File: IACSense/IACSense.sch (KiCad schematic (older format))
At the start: 61 parts, among them P1 IN, P2 OUT, P3 zcd, P4 event, P5 Prog, P6 nRF24L01+, P7 I2C, U1 MCP39F521, U2 MCP970x, U3 MCP1754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

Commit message: Update IACSense
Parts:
- added C21: 10u, Yame_library:SM0805-MR, symbol C
- added FB5: BLM18AG102SN1D, Yame_library:SM0603-MR, symbol FILTER
- R2: footprint Yame_library:SM0603-MR -> Yame_library:SM1206-MR
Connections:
- wire segments 180 -> 186
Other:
- moved on the sheet: C16, C19, C20, R18

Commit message: Update IACSense
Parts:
- removed P7: I2C, Yame_library:HE10_14-3C-2.54-MR, symbol CONN_01X03
- added P7: I2C, Yame_library:HE10_14-4C-2.54-MR, symbol CONN_01X04
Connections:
- wire segments 186 -> 189
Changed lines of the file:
@@
 $EndComp
 $Comp
-L CONN_01X03 P7
-U 1 1 5676C8C1
-P 10650 950
-F 0 "P7" H 10650 1150 50  0000 C CNN
-F 1 "I2C" V 10750 950 50  0000 C CNN
-F 2 "Yame_library:HE10_14-3C-2.54-MR" H 10650 950 50  0001 C CNN
-F 3 "" H 10650 950 50  0000 C CNN
-	1    10650 950
-	1    0    0    -1
-$EndComp
-$Comp
 L CONN_01X05 P5
 U 1 1 5676C91A
@@
 	2750 2400 3150 2400
 $Comp
-L GND #PWR1
+L GND #PWR01
 U 1 1 56D34A90
 P 2700 1900
-F 0 "#PWR1" H 2700 1650 50  0001 C CNN
+F 0 "#PWR01" H 2700 1650 50  0001 C CNN
 F 1 "GND" H 2700 1750 50  0000 C CNN
 F 2 "" H 2700 1900 60  0000 C CNN
@@
 Connection ~ 4000 2450
 $Comp
-L GND #PWR3
+L GND #PWR02
 U 1 1 56D35186
 P 3750 2900
-F 0 "#PWR3" H 3750 2650 50  0001 C CNN
+F 0 "#PWR02" H 3750 2650 50  0001 C CNN
 F 1 "GND" H 3750 2750 50  0000 C CNN
 F 2 "" H 3750 2900 60  0000 C CNN
@@
 Connection ~ 3350 3250
 $Comp
-L GND #PWR2
+L GND #PWR03
 U 1 1 56D35ED8
 P 3350 3850
-F 0 "#PWR2" H 3350 3600 50  0001 C CNN
+F 0 "#PWR03" H 3350 3600 50  0001 C CNN
 F 1 "GND" H 3350 3700 50  0000 C CNN
 F 2 "" H 3350 3850 60  0000 C CNN
@@
 $EndComp
 $Comp
-L GND #PWR4
+L GND #PWR04
 U 1 1 56D366F0
 P 3950 4700
-F 0 "#PWR4" H 3950 4450 50  0001 C CNN
+F 0 "#PWR04" H 3950 4450 50  0001 C CNN
 F 1 "GND" H 3950 4550 50  0000 C CNN
 F 2 "" H 3950 4700 60  0000 C CNN
@@
 $EndComp
 $Comp
-L GND #PWR7
+L GND #PWR05
 U 1 1 56D36767
 P 4250 4700
-F 0 "#PWR7" H 4250 4450 50  0001 C CNN
+F 0 "#PWR05" H 4250 4450 50  0001 C CNN
 F 1 "GND" H 4250 4550 50  0000 C CNN
 F 2 "" H 4250 4700 60  0000 C CNN
@@
 $EndComp
 $Comp
-L GND #PWR12
+L GND #PWR06
 U 1 1 56D37BE1
 P 6000 2700
-F 0 "#PWR12" H 6000 2450 50  0001 C CNN
+F 0 "#PWR06" H 6000 2450 50  0001 C CNN
 F 1 "GND" H 6000 2550 50  0000 C CNN
 F 2 "" H 6000 2700 60  0000 C CNN
@@
 Connection ~ 5850 3550
 $Comp
-L GND #PWR8
+L GND #PWR07
 U 1 1 56D38721
 P 4900 4250
-F 0 "#PWR8" H 4900 4000 50  0001 C CNN
+F 0 "#PWR07" H 4900 4000 50  0001 C CNN
 F 1 "GND" H 4900 4100 50  0000 C CNN
 F 2 "" H 4900 4250 60  0000 C CNN
@@
 $EndComp
 $Comp
-L GND #PWR9
+L GND #PWR08
 U 1 1 56D3887C
 P 5000 4450
-F 0 "#PWR9" H 5000 4200 50  0001 C CNN
+F 0 "#PWR08" H 5000 4200 50  0001 C CNN
 F 1 "GND" H 5000 4300 50  0000 C CNN
 F 2 "" H 5000 4450 60  0000 C CNN
@@
 $EndComp
 $Comp
-L GND #PWR10
+L GND #PWR09
 U 1 1 56D38905
 P 5200 4250
-F 0 "#PWR10" H 5200 4000 50  0001 C CNN
+F 0 "#PWR09" H 5200 4000 50  0001 C CNN
 F 1 "GND" H 5200 4100 50  0000 C CNN
 F 2 "" H 5200 4250 60  0000 C CNN
@@
 	5200 4200 5200 4250
 $Comp
-L GND #PWR11
+L GND #PWR010
 U 1 1 56D38BD8
 P 5850 4200
-F 0 "#PWR11" H 5850 3950 50  0001 C CNN
+F 0 "#PWR010" H 5850 3950 50  0001 C CNN
 F 1 "GND" H 5850 4050 50  0000 C CNN
 F 2 "" H 5850 4200 60  0000 C CNN
@@
 $EndComp
 $Comp
-L GND #PWR13
+L GND #PWR011
 U 1 1 56D38CDF
 P 6150 4200
-F 0 "#PWR13" H 6150 3950 50  0001 C CNN
+F 0 "#PWR011" H 6150 3950 50  0001 C CNN
 F 1 "GND" H 6150 4050 50  0000 C CNN
 F 2 "" H 6150 4200 60  0000 C CNN
@@
 $EndComp
 $Comp
-L GND #PWR17
+L GND #PWR012
 U 1 1 56D3A7BB
 P 6750 4300
-F 0 "#PWR17" H 6750 4050 50  0001 C CNN
+F 0 "#PWR012" H 6750 4050 50  0001 C CNN
 F 1 "GND" H 6750 4150 50  0000 C CNN
 F 2 "" H 6750 4300 60  0000 C CNN
@@
 $EndComp
 $Comp
-L GND #PWR20
+L GND #PWR013
 U 1 1 56D3A84D
 P 7150 4550
-F 0 "#PWR20" H 7150 4300 50  0001 C CNN
+F 0 "#PWR013" H 7150 4300 50  0001 C CNN
 F 1 "GND" H 7150 4400 50  0000 C CNN
 F 2 "" H 7150 4550 60  0000 C CNN
@@
 $EndComp
 $Comp
-L GND #PWR24
+L GND #PWR014
 U 1 1 56D3A8DF
 P 8000 4550
-F 0 "#PWR24" H 8000 4300 50  0001 C CNN
+F 0 "#PWR014" H 8000 4300 50  0001 C CNN
 F 1 "GND" H 8000 4400 50  0000 C CNN
 F 2 "" H 8000 4550 60  0000 C CNN
@@
 $EndComp
 $Comp
-L GND #PWR14
+L GND #PWR015
 U 1 1 56D3BEF2
 P 6200 7050
-F 0 "#PWR14" H 6200 6800 50  0001 C CNN
+F 0 "#PWR015" H 6200 6800 50  0001 C CNN
 F 1 "GND" H 6200 6900 50  0000 C CNN
 F 2 "" H 6200 7050 60  0000 C CNN
@@
 $EndComp
 $Comp
-L GND #PWR16
+L GND #PWR016
 U 1 1 56D3C09D
 P 6550 6100
-F 0 "#PWR16" H 6550 5850 50  0001 C CNN
+F 0 "#PWR016" H 6550 5850 50  0001 C CNN
 F 1 "GND" H 6550 5950 50  0000 C CNN
 F 2 "" H 6550 6100 60  0000 C CNN
@@
 $EndComp
 $Comp
-L GND #PWR18
+L GND #PWR017
 U 1 1 56D3C144
 P 6800 6100
-F 0 "#PWR18" H 6800 5850 50  0001 C CNN
+F 0 "#PWR017" H 6800 5850 50  0001 C CNN
 F 1 "GND" H 6800 5950 50  0000 C CNN
 F 2 "" H 6800 6100 60  0000 C CNN
@@
 $EndComp
 $Comp
-L GND #PWR21
+L GND #PWR018
 U 1 1 56D3C1EB
 P 7350 6150
-F 0 "#PWR21" H 7350 5900 50  0001 C CNN
+F 0 "#PWR018" H 7350 5900 50  0001 C CNN
 F 1 "GND" H 7350 6000 50  0000 C CNN
 F 2 "" H 7350 6150 60  0000 C CNN
@@
 $EndComp
 $Comp
-L GND #PWR25
+L GND #PWR019
 U 1 1 56D3C292
 P 8000 6150
-F 0 "#PWR25" H 8000 5900 50  0001 C CNN
+F 0 "#PWR019" H 8000 5900 50  0001 C CNN
 F 1 "GND" H 8000 6000 50  0000 C CNN
 F 2 "" H 8000 6150 60  0000 C CNN
@@
 $EndComp
 $Comp
-L GND #PWR15
+L GND #PWR020
 U 1 1 56D3C339
 P 6550 1200
-F 0 "#PWR15" H 6550 950 50  0001 C CNN
+F 0 "#PWR020" H 6550 950 50  0001 C CNN
 F 1 "GND" H 6550 1050 50  0000 C CNN
 F 2 "" H 6550 1200 60  0000 C CNN
@@
 $EndComp
 $Comp
-L GND #PWR5
+L GND #PWR021
 U 1 1 56D3C47C
 P 4000 1050
-F 0 "#PWR5" H 4000 800 50  0001 C CNN
+F 0 "#PWR021" H 4000 800 50  0001 C CNN
 F 1 "GND" H 4000 900 50  0000 C CNN
 F 2 "" H 4000 1050 60  0000 C CNN
@@
 $EndComp
 $Comp
-L GND #PWR6
+L GND #PWR022
 U 1 1 56D3C523
 P 4250 1050
-F 0 "#PWR6" H 4250 800 50  0001 C CNN
+F 0 "#PWR022" H 4250 800 50  0001 C CNN
 F 1 "GND" H 4250 900 50  0000 C CNN
 F 2 "" H 4250 1050 60  0000 C CNN
@@
 	7750 1150 7750 1250
 $Comp
-L GND #PWR22
+L GND #PWR023
 U 1 1 56D37A29
 P 7750 1250
-F 0 "#PWR22" H 7750 1000 50  0001 C CNN
+F 0 "#PWR023" H 7750 1000 50  0001 C CNN
 F 1 "GND" H 7750 1100 50  0000 C CNN
 F 2 "" H 7750 1250 60  0000 C CNN
@@
 $EndComp
 $Comp
-L GND #PWR26
+L GND #PWR024
 U 1 1 56D3842E
 P 8300 3700
-F 0 "#PWR26" H 8300 3450 50  0001 C CNN
+F 0 "#PWR024" H 8300 3450 50  0001 C CNN
 F 1 "GND" H 8300 3550 50  0000 C CNN
 F 2 "" H 8300 3700 60  0000 C CNN
@@
 $EndComp
 $Comp
-L GND #PWR27
+L GND #PWR025
 U 1 1 56D38434
 P 8600 3700
-F 0 "#PWR27" H 8600 3450 50  0001 C CNN
+F 0 "#PWR025" H 8600 3450 50  0001 C CNN
 F 1 "GND" H 8600 3550 50  0000 C CNN
 F 2 "" H 8600 3700 60  0000 C CNN
@@
 	8300 3600 8300 3700
 $Comp
-L GND #PWR28
+L GND #PWR026
 U 1 1 56D3877B
 P 9000 3050
-F 0 "#PWR28" H 9000 2800 50  0001 C CNN
+F 0 "#PWR026" H 9000 2800 50  0001 C CNN
 F 1 "GND" H 9000 2900 50  0000 C CNN
 F 2 "" H 9000 3050 60  0000 C CNN
@@
 Wire Wire Line
 	9000 3000 9000 3050
-Text Label 9100 1050 0    60   ~ 0
-3.3D
-Wire Wire Line
-	9000 1050 9300 1050
 Wire Wire Line
 	9000 1050 9000 1200
@@
 $EndComp
 $Comp
-L GND #PWR23
+L GND #PWR027
 U 1 1 56D39A08
 P 7800 3100
-F 0 "#PWR23" H 7800 2850 50  0001 C CNN
+F 0 "#PWR027" H 7800 2850 50  0001 C CNN
 F 1 "GND" H 7800 2950 50  0000 C CNN
 F 2 "" H 7800 3100 60  0000 C CNN
@@
 MISO
 $Comp
-L GND #PWR29
+L GND #PWR028
 U 1 1 56DBAE1A
 P 10350 4600
-F 0 "#PWR29" H 10350 4350 50  0001 C CNN
+F 0 "#PWR028" H 10350 4350 50  0001 C CNN
 F 1 "GND" H 10350 4450 50  0000 C CNN
 F 2 "" H 10350 4600 60  0000 C CNN
@@
 Connection ~ 7800 2450
 $Comp
-L GND #PWR30
+L GND #PWR029
 U 1 1 56DBE06C
 P 10400 1150
-F 0 "#PWR30" H 10400 900 50  0001 C CNN
+F 0 "#PWR029" H 10400 900 50  0001 C CNN
 F 1 "GND" H 10400 1000 50  0000 C CNN
 F 2 "" H 10400 1150 60  0000 C CNN
@@
 $EndComp
 $Comp
-L GND #PWR19
+L GND #PWR030
 U 1 1 57743D9C
 P 6850 1200
-F 0 "#PWR19" H 6850 950 50  0001 C CNN
+F 0 "#PWR030" H 6850 950 50  0001 C CNN
 F 1 "GND" H 6850 1050 50  0000 C CNN
 F 2 "" H 6850 1200 60  0000 C CNN
@@
 	6900 3450 6900 2050
 Connection ~ 7650 4100
+$Comp
+L CONN_01X04 P7
+U 1 1 57842388
+P 10650 900
+F 0 "P7" H 10650 1150 50  0000 C CNN
+F 1 "I2C" V 10750 900 50  0000 C CNN
+F 2 "Yame_library:HE10_14-4C-2.54-MR" H 10650 900 50  0001 C CNN
+F 3 "" H 10650 900 50  0000 C CNN
+	1    10650 900
+	1    0    0    -1
+$EndComp
+Wire Wire Line
+	9000 1050 9300 1050
+Text Label 9100 1050 0    60   ~ 0
+3.3D
+Wire Wire Line
+	10150 750  10450 750
+Text Label 10150 750  0    60   ~ 0
+3.3D
+$Comp
+L GND #PWR031
+U 1 1 57843F08
+P 8850 3050
+F 0 "#PWR031" H 8850 2800 50  0001 C CNN
+F 1 "GND" H 8850 2900 50  0000 C CNN
+F 2 "" H 8850 3050 60  0000 C CNN
+F 3 "" H 8850 3050 60  0000 C CNN
+	1    8850 3050
+	1    0    0    -1
+$EndComp
+Wire Wire Line
+	8850 3000 8850 3050
+$Comp
+L GND #PWR?
+U 1 1 57844CD3
+P 4800 4450
+F 0 "#PWR?" H 4800 4200 50  0001 C CNN
+F 1 "GND" H 4800 4300 50  0000 C CNN
+F 2 "" H 4800 4450 60  0000 C CNN
+F 3 "" H 4800 4450 60  0000 C CNN
+	1    4800 4450
+	1    0    0    -1
+$EndComp
+Wire Wire Line
+	4800 4200 4800 4450
 $EndSCHEMATC

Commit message: Add DAC analog
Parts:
- D3: symbol LED -> LED-RESCUE-IACSense
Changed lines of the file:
@@
 	6900 2050 8000 2050
 $Comp
-L LED D3
+L LED-RESCUE-IACSense D3
 U 1 1 56D3975F
 P 8000 2650
@@
 96 6B B1 16 0C 5F EA 76 BB 5B C5 AD E5 B0 18 68 22 1A 3C 61 3F D3 65 7F 3A B3 5B 09 75 D6 E6 1C
 11 19 10 99 F7 1E 0D C3 30 8C E3 24 2C EB F1 9E 9E ED E2 D6 E6 46 61 6D 25 8F 88 42 70 D7 CB B4
-E7 3A 1A B3 D9 F4 9B 3F 01 3A 98 FB 92 40 BB C0 C4 00 00 00 00 49 45 4E 44 AE 42 60 82 00
+E7 3A 1A B3 D9 F4 9B 3F 01 3A 98 FB 92 40 BB C0 C4 00 00 00 00 49 45 4E 44 AE 42 60 82
 EndData
 $EndBitmap

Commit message: Update IACSense
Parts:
- removed C10: CP, Capacitors_ThroughHole:C_Radial_D14_L25_P5, symbol CP
- removed C11: 10u, Yame_library:SM0805-MR, symbol C
- removed C13: 100n, Yame_library:SM0603-MR, symbol C
- removed C3: 0.68uF_X2_B32922C3684M, Yame_library:X2_15mm, symbol C
- removed D1: MB8S, Yame_library:MBxS, symbol Diode_Bridge-RESCUE-IACSense
- removed D2: BZX85C4V7, Yame_library:DO-204AL, symbol ZENER
- removed F1: 0751.0062, Yame_library:Fuse_5x20, symbol FUSE_CLIP_5x20
- removed P6: nRF24L01+, Yame_library:NRF24L01+, symbol CONN_02X04
- removed R1: LRMAM1206-R002FT5, Yame_library:SM1206-MR, symbol R
- removed R19, R8: R, Yame_library:SM0603-MR, symbol R
- removed R2: 100_0.5W_1206, Yame_library:SM1206-MR, symbol R
- removed R20: 33, Yame_library:SM0603-MR, symbol R
- added C? (x2): 1u_400V, symbol CP
- added C?: 100n, symbol C
- added C?: 10u, symbol C
- added C?: 100u_25V, symbol CP
- added C?: C, symbol C
- added C?: 1u, Yame_library:SM0805-MR, symbol C
- added D? (x3): 1N4007, symbol D
- added D?: UF4005, symbol D
- added D?: Q_TRIAC_AAG, symbol Q_TRIAC_AAG
- added FB?: BLM18AG102SN1D, Yame_library:SM0603-MR, symbol FILTER
- added L?: RLB0914-681KL, symbol L
- added R?: FC4L32R002GER, symbol R_Shunt
- added R?: EMC2-8R2K, symbol R
- added R?: 100, symbol R
- added R?: 100k, symbol R
- added R?: 2.49k, symbol R
- added R?: 3.48k, symbol R
- added R?: 1.6k, symbol R
- added R? (x4): R, symbol R
- added R? (x2): 680, Yame_library:SM0603-MR, symbol R
- added SW?: SW_Push, symbol SW_Push
- added U?: HC-05_Bluetooth_Module, symbol HC-05_Bluetooth_Module
- added U?: LNK320x, symbol LNK320x
- added U?: MOC3021M, symbol MOC3021M
- U3: value MCP1754 -> MCP1754ST-3302E/CB
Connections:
- net labels added: +5V, Out_SW, Rx_BL, Tx_BL
- net labels removed: /CS, MISO, MOSI, SCK
- wire segments 189 -> 233
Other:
- note removed: "18*11*18.5"
- note removed: "BZX85C4V7\nZMM5230B\n"
- moved on the sheet: C1, C12, C14, C15, C16, C17, C18, C19, C2, C20, C21, C4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

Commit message: Update IACSense footprint
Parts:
- added C10: 100n, Capacitors_THT:C_Rect_L16.5mm_W10.7mm_P15.00mm_MKT, symbol C
- added C3: 100n, Capacitors_THT:C_Rect_L11.0mm_W4.2mm_P10.00mm_MKT, symbol C
- added R19: 2.4k, Resistors_THT:R_Axial_DIN0414_L11.9mm_D4.5mm_P5.08mm_Vertical, symbol R
- C22: renamed from C?; footprint (none) -> Yame_library:SM0603-MR
- C23: renamed from C?; footprint (none) -> Yame_library:SM0805-MR
- D2, D4, D5, D6: renamed from D?; footprint (none) -> Diodes_THT:D_DO-41_SOD81_P7.62mm_Horizontal
- L1: renamed from L?; footprint (none) -> Inductors_THT:L_Radial_D10.0mm_P5.00mm_Fastron_07M
- P5: footprint Yame_library:HE10_14-5C-2.54-MR -> Pin_Headers:Pin_Header_Straight_1x05_Pitch2.54mm
- R18: value 100 -> 10k
- R22, R23, R24, R25: renamed from R?; footprint (none) -> Yame_library:SM0603-MR
- R8: renamed from R?; footprint Yame_library:SM0603-MR -> Resistors_THT:R_Axial_DIN0414_L11.9mm_D4.5mm_P5.08mm_Vertical
- U5: renamed from U?; footprint (none) -> Housings_DIP:DIP-6_W7.62mm
- U6: renamed from U?; footprint (none) -> Yame_library:SO-8C-7
- gave numbers to parts that had none: 17
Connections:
- wire segments 233 -> 240
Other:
- moved on the sheet: R1, R8, U5

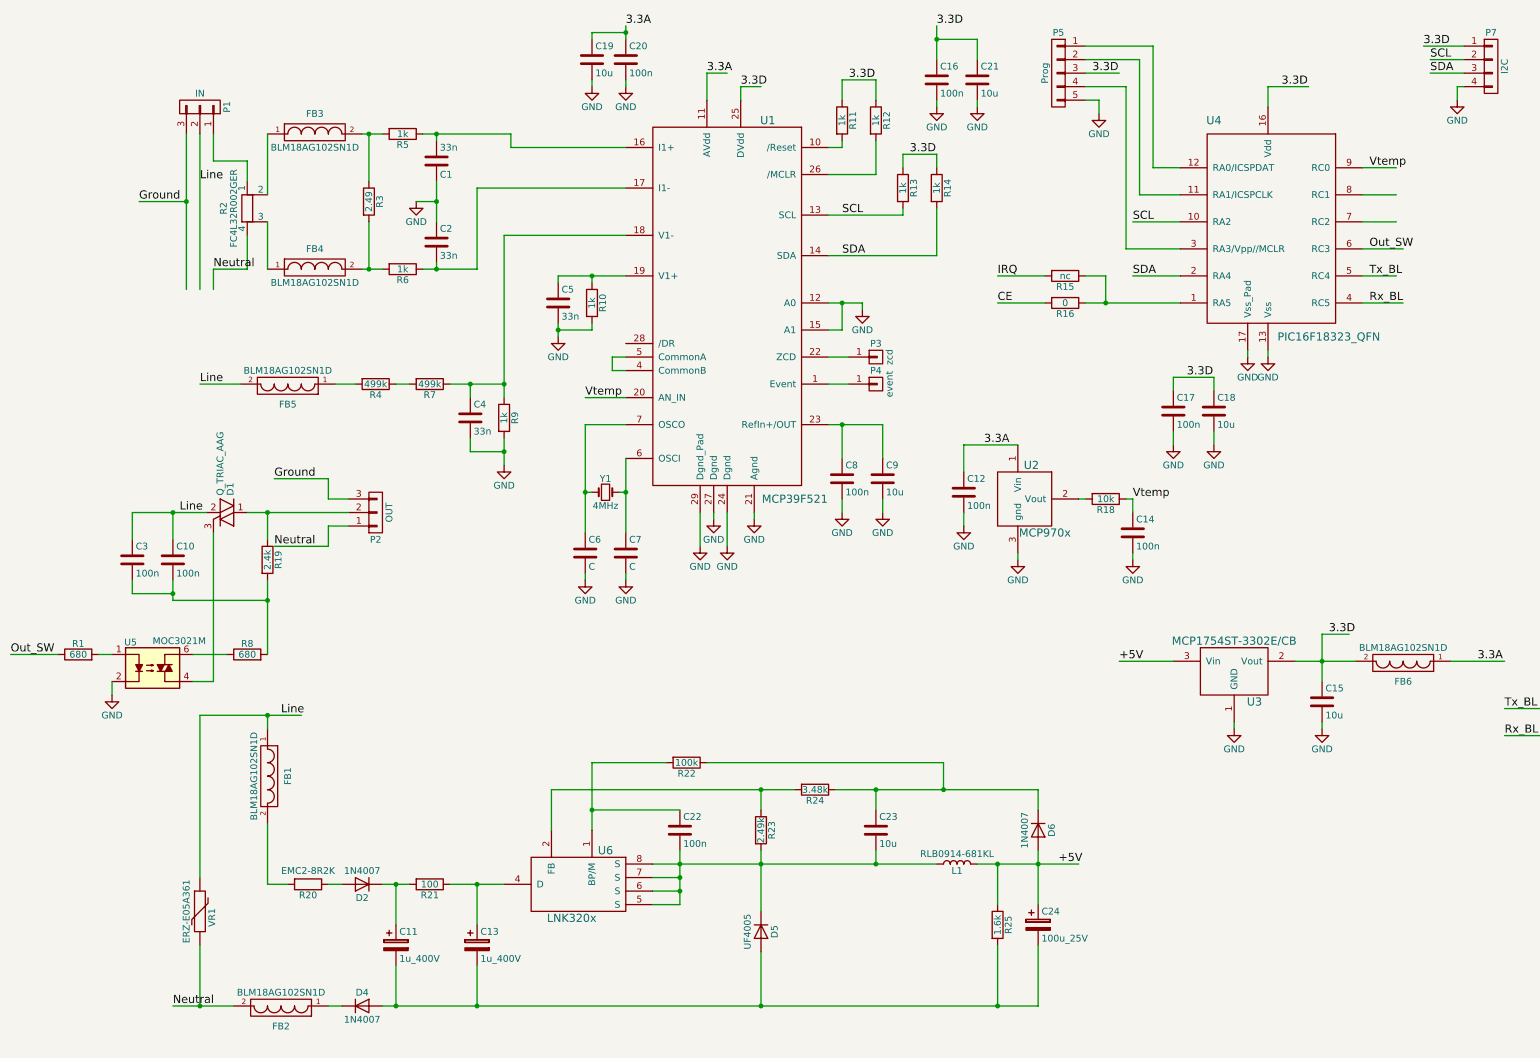
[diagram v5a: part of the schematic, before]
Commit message: Update IACSense layout
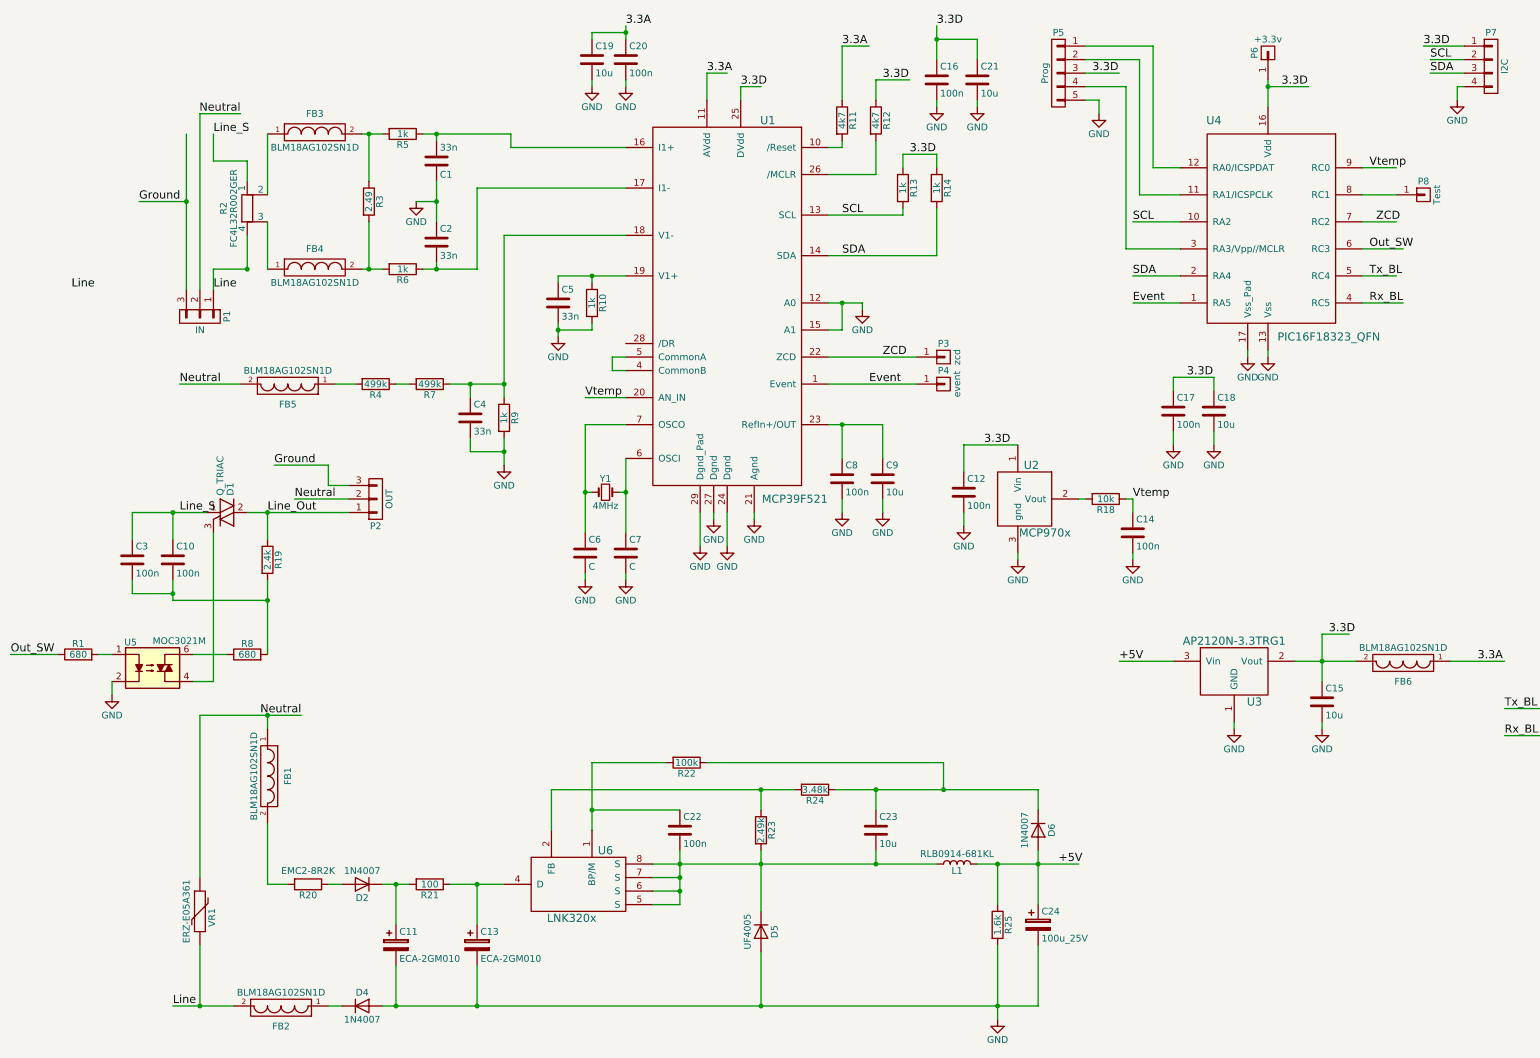
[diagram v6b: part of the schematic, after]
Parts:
- removed D1: Q_TRIAC_AAG, symbol Q_TRIAC_AAG
- removed R15: nc, Yame_library:SM0603-MR, symbol R
- removed R16: 0, Yame_library:SM0603-MR, symbol R
- added D1: Q_TRIAC, TO_SOT_Packages_THT:TO-220-3_Vertical, symbol Q_TRIAC
- added P6: +3.3v, Pin_Headers:Pin_Header_Straight_1x01_Pitch1.00mm, symbol CONN_01X01
- added P8: Test, Pin_Headers:Pin_Header_Straight_1x01_Pitch1.00mm, symbol CONN_01X01
- C11, C13: value 1u_400V -> ECA-2GM010; footprint (none) -> Capacitors_THT:CP_Radial_D6.3mm_P2.50mm
- C24: footprint (none) -> Capacitors_THT:CP_Radial_D6.3mm_P2.50mm
- C25, R26, R27, R28, R29: footprint (none) -> Yame_library:SM0603-MR
- D3: footprint LEDs:LED_0603 -> Yame_library:SM0603-LED-MR
- L1: footprint Inductors_THT:L_Radial_D10.0mm_P5.00mm_Fastron_07M -> Inductors_THT:L_Radial_D8.7mm_P5.00mm_Fastron_07HCP
- P3, P4: footprint Yame_library:Test_Point_T_H -> Pin_Headers:Pin_Header_Straight_1x01_Pitch1.00mm
- P7: footprint Yame_library:HE10_14-4C-2.54-MR -> Pin_Headers:Pin_Header_Straight_1x04_Pitch1.00mm
- R11, R12: value 1k -> 4k7
- R2: footprint (none) -> FC4L32
- R20: footprint (none) -> Resistors_THT:R_Axial_DIN0414_L11.9mm_D4.5mm_P5.08mm_Vertical
- R21: footprint (none) -> Yame_library:SM0805-MR
- SW1: footprint (none) -> Buttons_Switches_SMD:SW_SPST_FSMSM
- U3: value MCP1754ST-3302E/CB -> AP2120N-3.3TRG1
- U7: footprint (none) -> Yame_library:HM-10_BLE
- Y1: footprint Crystals:Q_49U3HMS -> Crystals:Crystal_HC49-4H_Vertical
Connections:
- net labels added: Event, Line_Out, Line_S, ZCD
- net labels removed: CE, IRQ
- wire segments 240 -> 236
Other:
- moved on the sheet: P1, P2, P3, P4
